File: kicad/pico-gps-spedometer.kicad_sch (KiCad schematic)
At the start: 19 parts, among them J1 Akkumulátor be, J2 TP4056-18650-Charger, J3 uBlox NEO GPS (6M/8M), Q1 PN2222A, U1 RP2040-ZERO, U2 DS18B20, U3 LM7805_TO220, U4 TFT_320x240

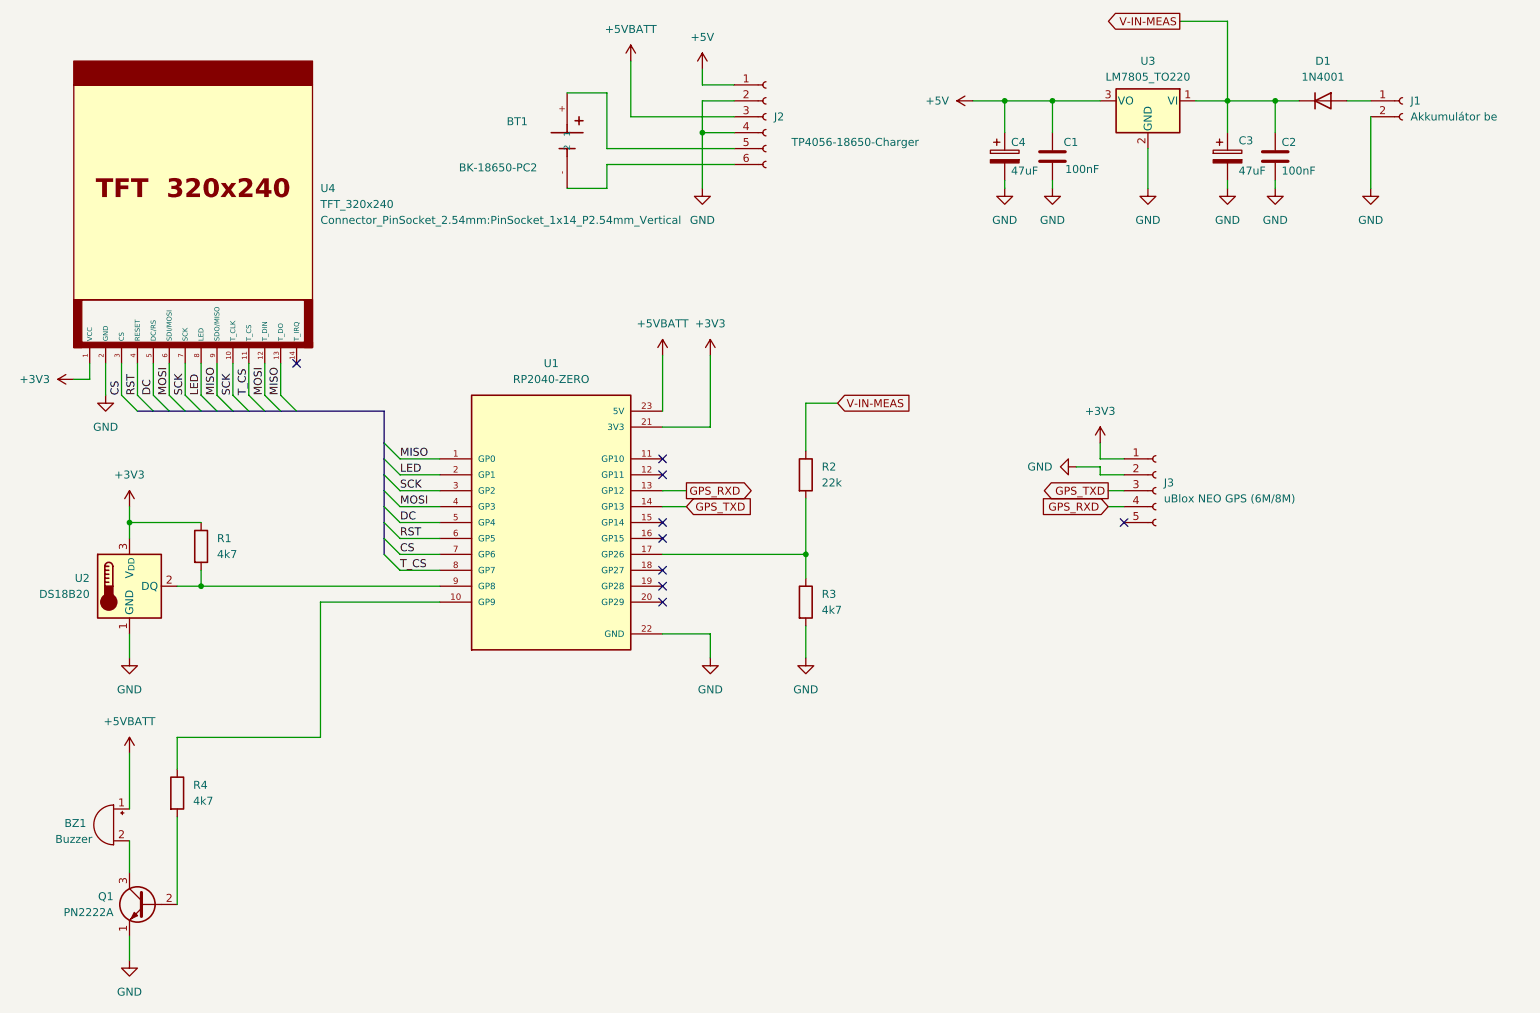
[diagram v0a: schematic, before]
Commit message: Add TFT backlight adjustment and utility functions
- Implemented TftBackLightAdjuster for dynamic LED backlight control based on ambient light sensor readings.
- Added utility functions for TFT touch calibration and sound feedback (beepTick and beepError) in Utils.cpp.
- Included necessary headers and defined constants for sensor thresholds and brightness levels.
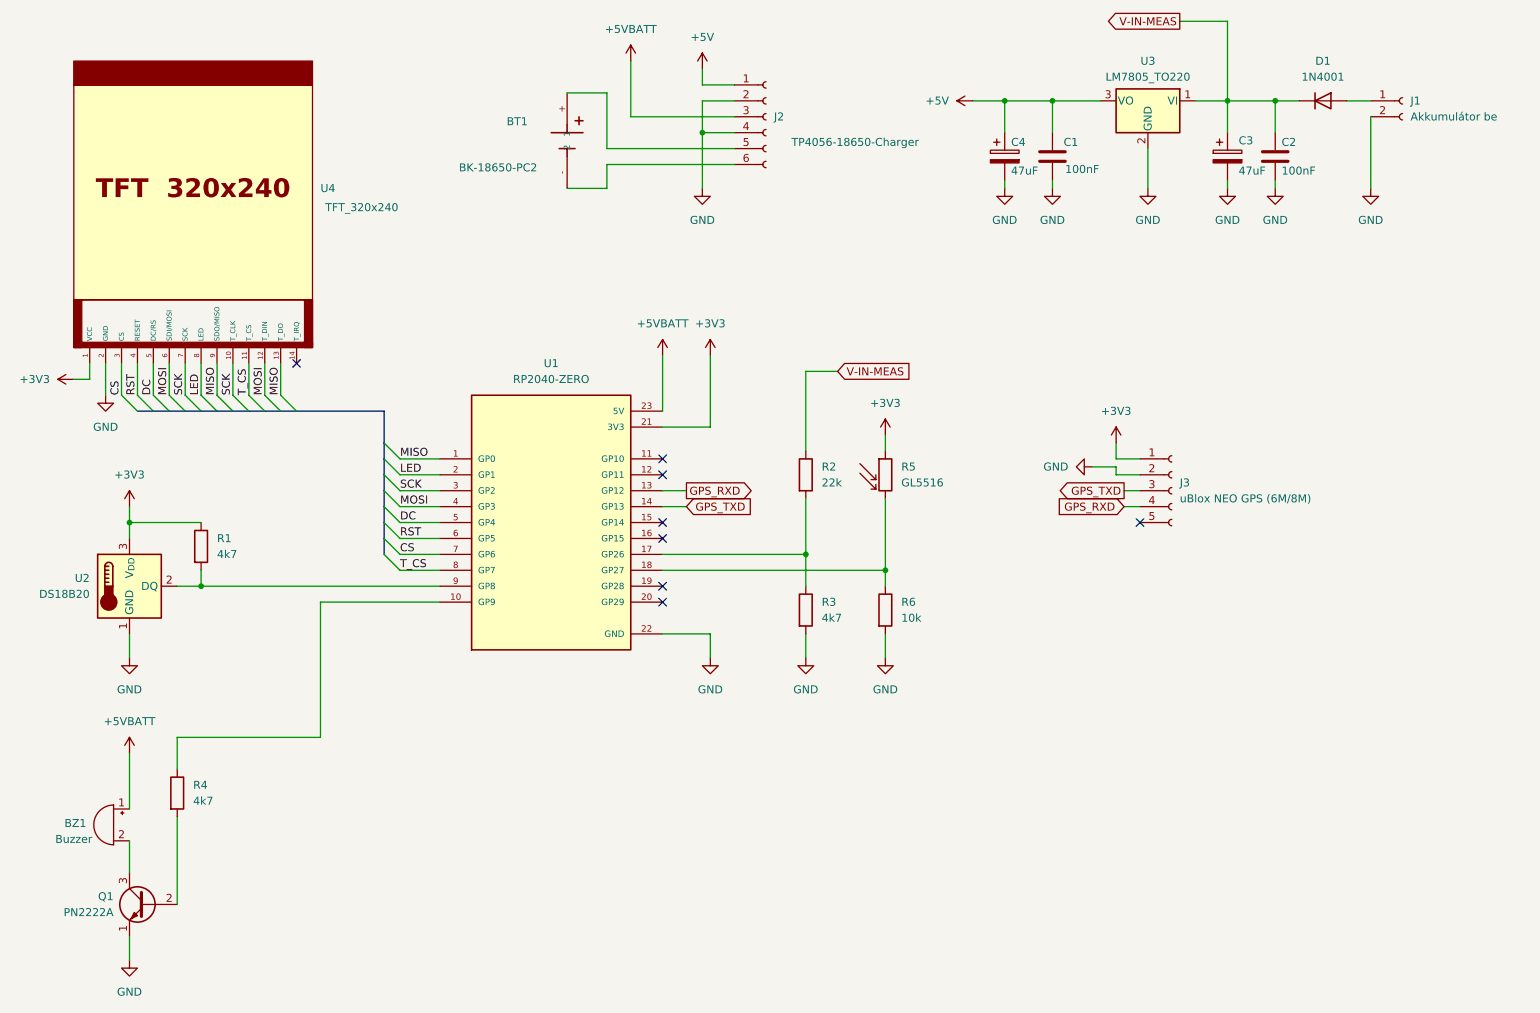
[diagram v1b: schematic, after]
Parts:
- added R5: GL5516, OptoDevice:R_LDR_4.9x4.2mm_P2.54mm_Vertical, symbol Device:R_Photo
- added R6: 10k, Resistor_THT:R_Axial_DIN0204_L3.6mm_D1.6mm_P7.62mm_Horizontal, symbol Device:R
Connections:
- net +3V3: now also R5.1
- net GND: now also R6.2
- net at U1.18 (GP27): now also R5.2, R6.1
- no-connect marks 9 -> 8
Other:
- moved on the sheet: J3, R3
